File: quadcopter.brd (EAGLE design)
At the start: 203.5 x 203.5 mm, 73 parts, among them J1 AVR_SPI_PRG_6NS, U3 ATMEGA128RFA1

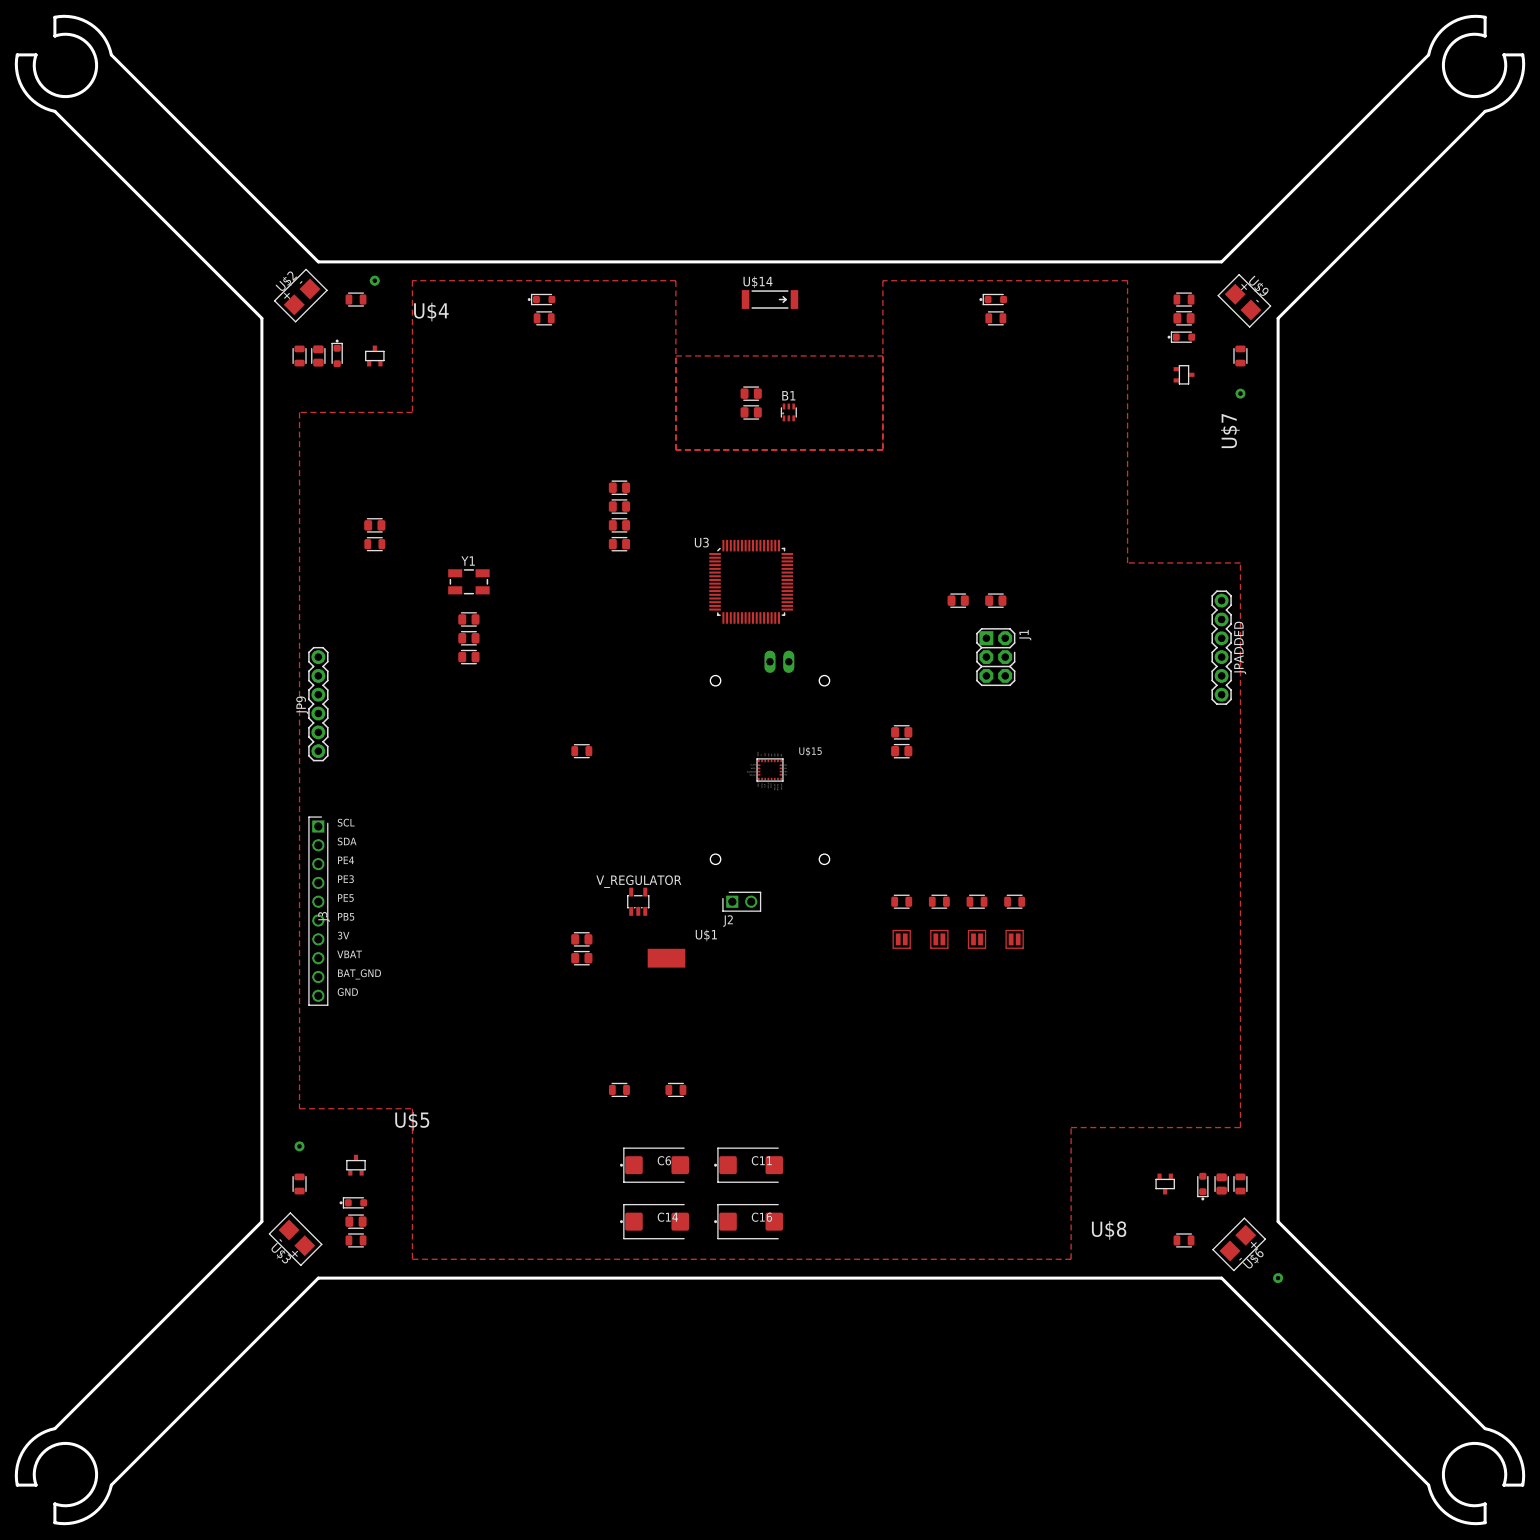
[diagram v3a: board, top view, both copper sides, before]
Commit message: made changes to pour
need to change RED LED to be more like data sheet
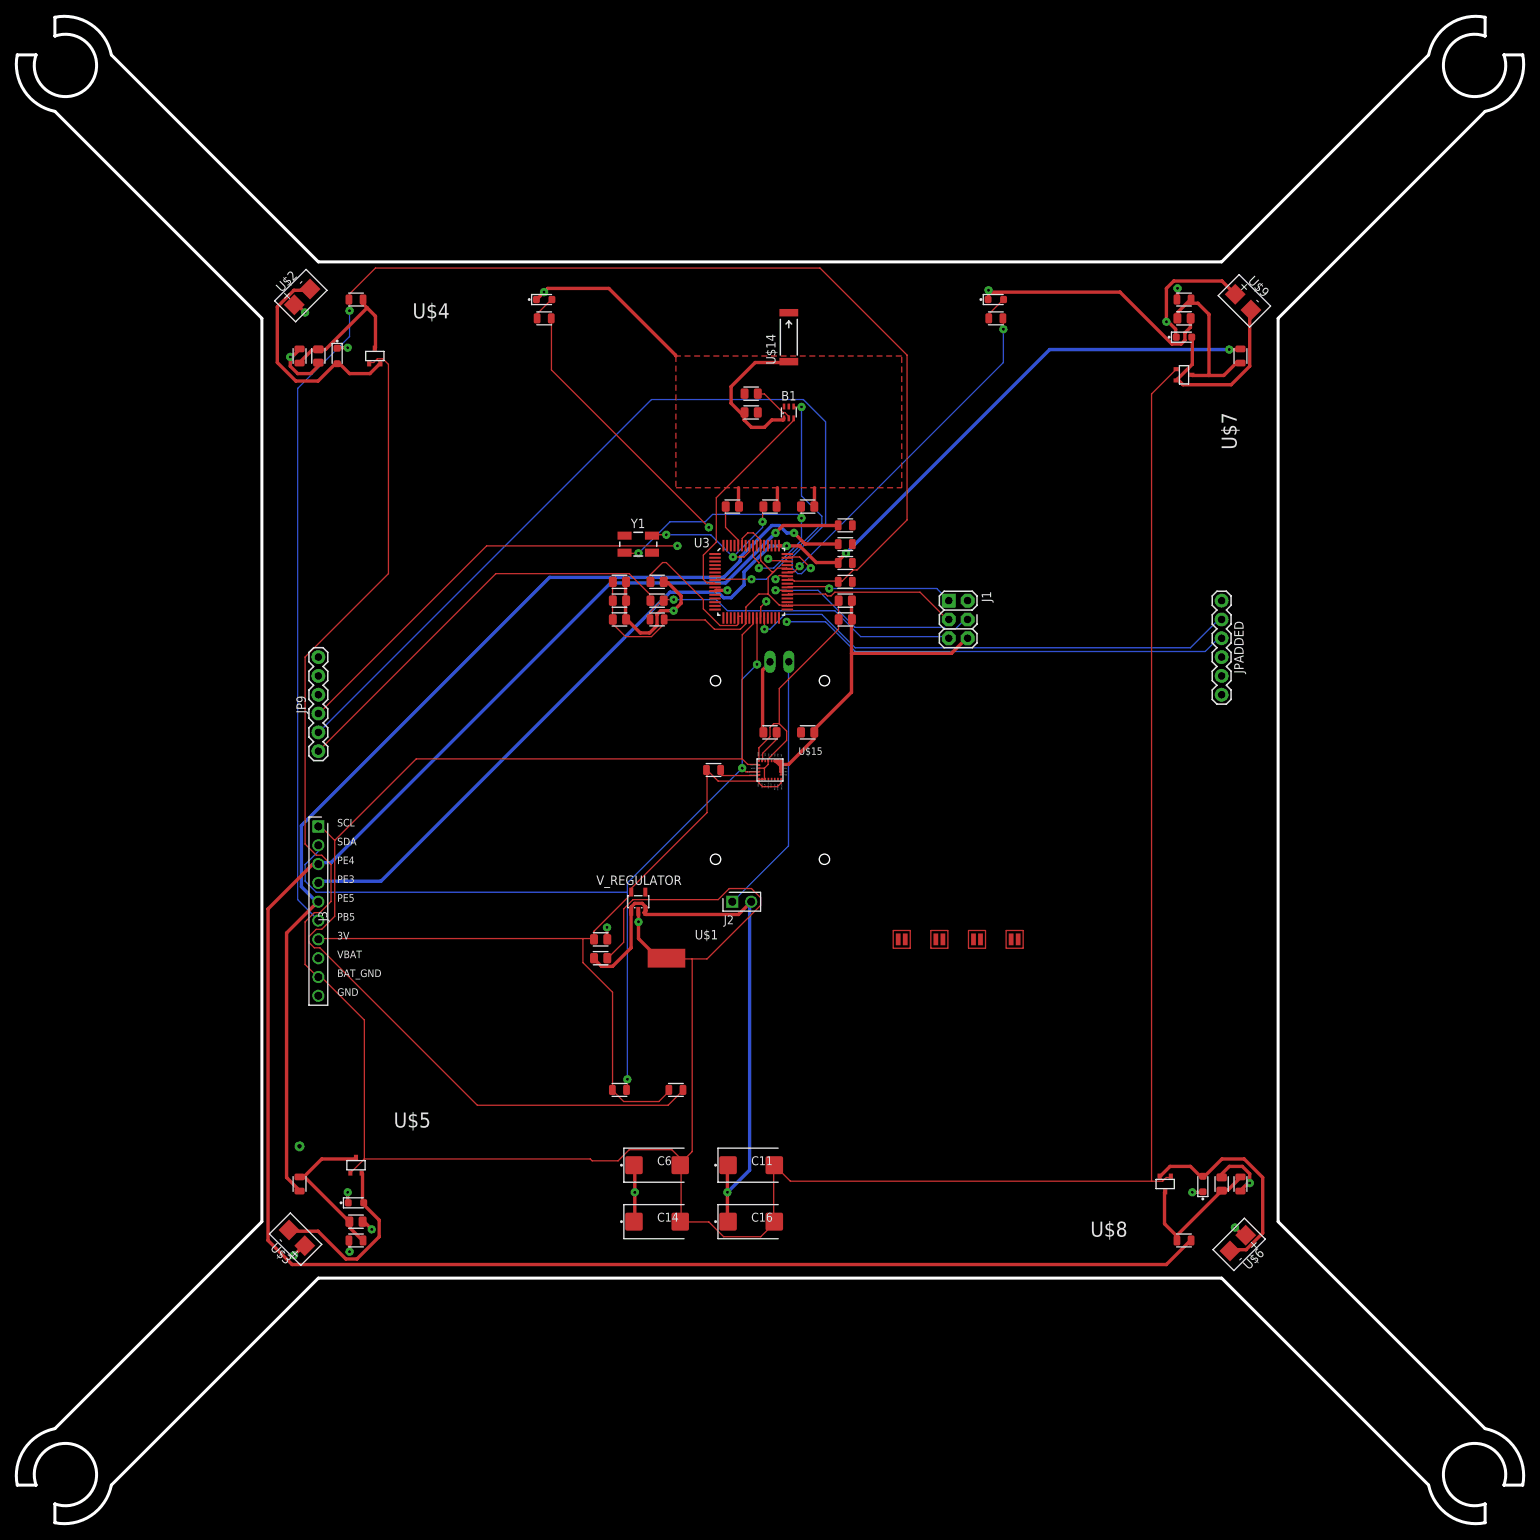
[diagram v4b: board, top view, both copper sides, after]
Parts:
- moved R1 51.4 mm to (10.2, 30.5)
- moved R8 51.4 mm to (10.2, 33.0)
- moved R15 48.9 mm to (10.2, 25.4)
- moved R7 47.5 mm to (10.2, 27.9)
- moved C1 39.4 mm to (-15.2, 22.9)
- moved R11 39.4 mm to (-15.2, 20.3)
- moved C9 25.5 mm to (5.08, 35.6)
- moved Y1 23.4 mm to (-17.8, 30.5)
- moved C2 20.9 mm to (-20.3, 22.9)
- moved C27 20.9 mm to (-20.3, 25.4)
- moved C28 20.9 mm to (-20.3, 20.3)
- moved C20 20.5 mm to (10.2, 20.3)
- moved C12 20.3 mm to (0.00, 35.6)
- moved R18 18.0 mm to (-7.62, 0.00)
- moved C8 17.8 mm to (0.00, 5.08)
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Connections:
- net FILTEREDNE: now also C15.1
- net FILTEREDNW: now also C10.1
- net FILTEREDSE: now also C17.1
- net FILTEREDSW: now also C13.1
- net PB5: no longer C10.1
- net PE3: no longer C17.1
- net PE4: no longer C15.1
- net PE5: no longer C13.1
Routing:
- net BAT_GND: track 0.00 -> 438.0 mm
- net PE4: track 0.00 -> 270.4 mm, vias 0 -> 1
- net PB5: track 0.00 -> 212.3 mm, vias 0 -> 1
- net 3V: track 0.00 -> 205.6 mm
- net GND: track 0.00 -> 173.6 mm, vias 0 -> 11
- net SCL: track 0.00 -> 161.1 mm
- net PE3: track 0.00 -> 159.1 mm, vias 0 -> 3
- net PE5: track 0.00 -> 143.8 mm, vias 0 -> 1
- net SDA: track 0.00 -> 123.2 mm, vias 0 -> 3
- net TX0: track 0.00 -> 116.8 mm, vias 0 -> 1
- net VCC: track 0.00 -> 114.3 mm, vias 0 -> 9
- net RX0: track 0.00 -> 76.4 mm, vias 0 -> 2
- net RX1: track 0.00 -> 67.7 mm, vias 0 -> 2
- net TX1: track 0.00 -> 67.7 mm, vias 0 -> 1
- net N$21: track 0.00 -> 56.7 mm
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- added copper zone on layer 2, net GND
- added copper zone on layer 2, net VCC
- removed copper zone on layer 15, net ANTENA
- removed copper zone on layer 1, net N$1
- removed copper zone on layer 2, net N$12
- removed copper zone on layer 2, net N$22
- removed copper zone on layer 2, net VBAT

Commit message: made changes to board, almost done.
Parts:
- U$10, U$11, U$12, U$13: device LEDs:RED_LED -> LEDs_new:RED_LED
- moved U$12 61.4 mm to (25.4, 38.1)
- moved U$11 61.2 mm to (27.9, 38.1)
- moved U$10 61.0 mm to (30.5, 38.1)
- moved U$13 61.0 mm to (33.0, 38.1)
- moved R17 46.4 mm to (-5.08, 2.54)
- moved R16 45.8 mm to (-5.08, 0.00)
- moved JP9 17.8 mm to (-61.0, 20.3)
- moved Y1 13.2 mm to (-4.94, 33.7), turned to 180 degrees
- moved C1 12.7 mm to (-7.62, 12.7), turned to 180 degrees
- moved R1 9.68 mm to (1.00, 33.6), turned to 90 degrees
- moved R11 9.16 mm to (-7.62, 15.2)
- moved J2 8.95 mm to (-13.4, -21.1)
- moved C27 8.58 mm to (-11.7, 25.4), turned to 90 degrees
- moved C7 8.03 mm to (5.08, 50.8)
- moved C2 7.02 mm to (-13.8, 25.4), turned to 90 degrees
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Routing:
- net BAT_GND: track 438.0 -> 0.00 mm
- net PE4: track 270.4 -> 0.00 mm, vias 1 -> 0
- net PB5: track 212.3 -> 0.00 mm, vias 1 -> 0
- net 3V: track 205.6 -> 0.00 mm
- net GND: track 173.6 -> 0.00 mm, vias 11 -> 0
- net SCL: track 161.1 -> 0.00 mm
- net PE3: track 159.1 -> 0.00 mm, vias 3 -> 0
- net PE5: track 143.8 -> 0.00 mm, vias 1 -> 0
- net SDA: track 123.2 -> 0.00 mm, vias 3 -> 0
- net TX0: track 116.8 -> 0.00 mm, vias 1 -> 0
- net VCC: track 114.3 -> 0.00 mm, vias 9 -> 0
- net RX0: track 76.4 -> 0.00 mm, vias 2 -> 0
- net RX1: track 67.7 -> 0.00 mm, vias 2 -> 0
- net TX1: track 67.7 -> 0.00 mm, vias 1 -> 0
- net N$21: track 56.7 -> 0.00 mm
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
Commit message: almost done with board, have 3 airwires
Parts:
- moved JP9 92.2 mm to (30.5, 8.13)
- moved U$13 58.1 mm to (12.8, -16.3)
- moved U$10 58.0 mm to (10.5, -16.3)
- moved U$11 57.9 mm to (8.21, -16.3)
- moved U$12 57.8 mm to (5.92, -16.3)
- moved D4 45.6 mm to (26.1, 23.9)
- moved U$3 45.4 mm to (-31.1, -31.7)
- moved D3 45.2 mm to (26.6, -23.8)
- moved U$6 45.0 mm to (32.0, -31.4)
- moved R2 44.9 mm to (-30.1, -25.9)
- moved U$9 44.4 mm to (31.4, 32.8)
- moved R5 43.6 mm to (-25.0, -32.7)
- moved R12 43.6 mm to (32.2, -25.6)
- moved R4 43.5 mm to (-33.7, 24.1)
- moved C13 43.4 mm to (-25.0, -30.4)
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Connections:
- net BAT_GND: now also BATT1.-, U$1.P$1; no longer U$1.P$2
- net GND: now also U$1.P$2; no longer BATT1.-, U$1.P$1
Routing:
- net GND: track 0.00 -> 242.8 mm, vias 0 -> 4
- net BAT_GND: track 0.00 -> 226.4 mm, vias 0 -> 2
- net PE4: track 0.00 -> 143.9 mm, vias 0 -> 4
- net 3V: track 0.00 -> 142.7 mm, vias 0 -> 3
- net PE3: track 0.00 -> 90.3 mm, vias 0 -> 1
- net PE5: track 0.00 -> 84.8 mm, vias 0 -> 2
- net VCC: track 0.00 -> 84.2 mm, vias 0 -> 10
- net PB5: track 0.00 -> 83.9 mm, vias 0 -> 1
- net SDA: track 0.00 -> 58.6 mm, vias 0 -> 2
- net SCL: track 0.00 -> 52.6 mm, vias 0 -> 1
- net N$21: track 0.00 -> 49.1 mm, vias 0 -> 1
- net RX1: track 0.00 -> 40.3 mm, vias 0 -> 2
- net PB6: track 0.00 -> 39.1 mm, vias 0 -> 2
- net RESET: track 0.00 -> 34.6 mm, vias 0 -> 1
- net N$9: track 0.00 -> 34.3 mm
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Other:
- board size 203.5 x 203.5 mm -> 137.4 x 137.4 mm

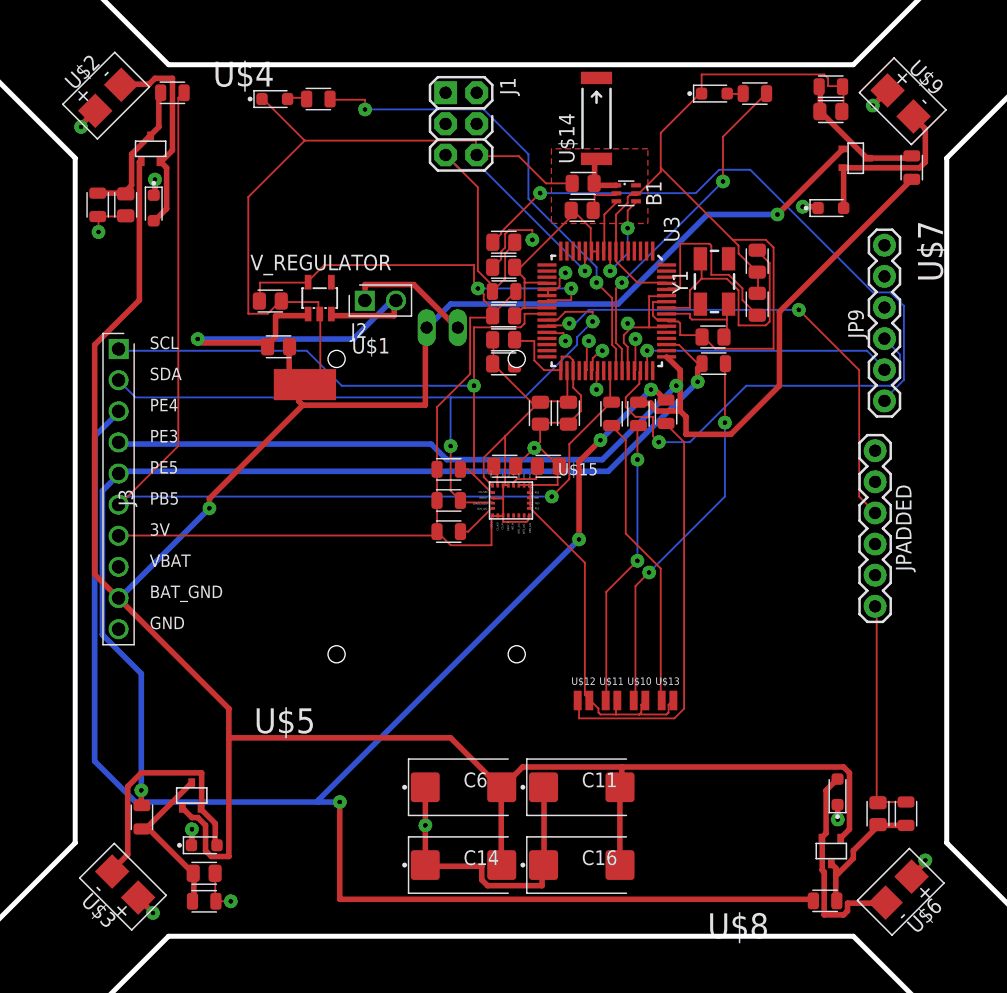
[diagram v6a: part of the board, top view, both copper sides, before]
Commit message: board 100% routed
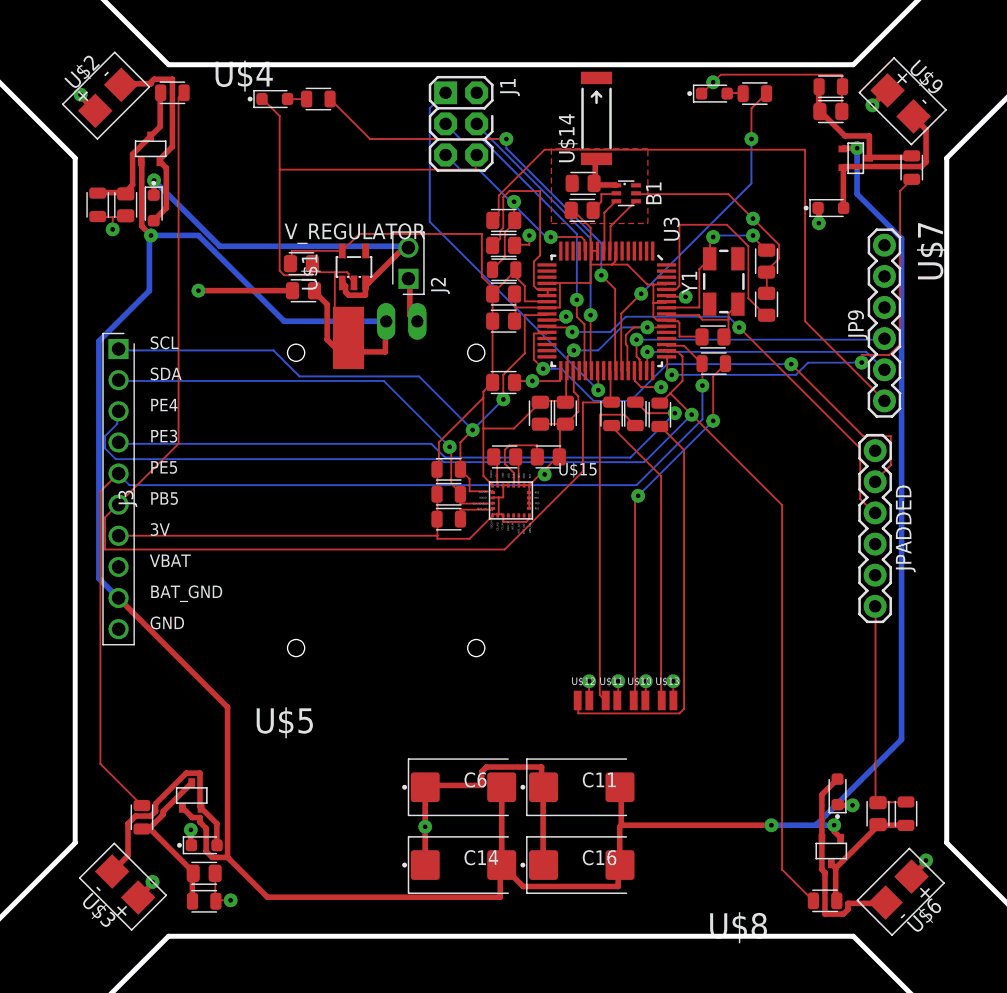
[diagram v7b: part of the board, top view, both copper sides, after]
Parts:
- moved U$1 5.57 mm to (-13.3, 14.5), turned to 90 degrees
- moved C3 5.00 mm to (-16.9, 17.1)
- moved J2 3.98 mm to (-8.37, 18.1), turned to 90 degrees
- moved C4 3.97 mm to (-17.1, 19.3)
- moved V_REGULATOR 3.78 mm to (-12.8, 19.1)
- moved BATT1 3.34 mm to (-10.2, 0.01)
- moved C27 1.78 mm to (-0.60, 16.9)
- moved C1 1.78 mm to (-0.58, 22.9)
- moved C18 1.78 mm to (-0.60, 20.8)
- moved R11 1.78 mm to (-0.56, 18.8)
- moved C2 1.52 mm to (-0.60, 14.6)
- moved C28 1.52 mm to (-0.60, 9.63)
- moved R18 1.02 mm to (-5.08, -1.52)
- moved C12 0.76 mm to (20.9, 19.5)
- moved C19 0.76 mm to (20.9, 16.0)
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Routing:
- net GND: track 242.8 -> 174.4 mm, vias 4 -> 12
- net PE4: track 143.9 -> 105.8 mm, vias 4 -> 1
- net RESET: track 34.6 -> 21.7 mm, vias 1 -> 2
- net 3V: track 142.7 -> 130.3 mm
- net RX0: track 33.8 -> 22.9 mm
- net TX1: track 32.2 -> 41.7 mm, vias 1 -> 2
- net MOSI: track 32.8 -> 24.0 mm
- net PB5: track 83.9 -> 92.2 mm, vias 1 -> 0
- net BAT_GND: track 226.4 -> 234.8 mm, vias 2 -> 4
- net N$3: track 21.5 -> 13.9 mm, vias 0 -> 2
- net VCC: track 84.2 -> 76.7 mm
- net N$6: track 10.3 -> 3.84 mm
- net SDA: track 58.6 -> 53.3 mm
- net DVDD: track 13.1 -> 17.2 mm, vias 2 -> 0
- net N$20: track 3.35 -> 6.96 mm
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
